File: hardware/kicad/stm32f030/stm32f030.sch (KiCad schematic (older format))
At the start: 5 parts, among them P1 CONN_01X02, U1 LM1117-3.3

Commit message: hardware/kicad/stm32f030: progress
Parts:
- P1: value CONN_01X02 -> 5VIN
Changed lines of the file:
@@
 P 4700 4500
 F 0 "P1" H 4700 4650 50  0000 C CNN
-F 1 "CONN_01X02" V 4800 4500 50  0000 C CNN
+F 1 "5VIN" V 4800 4500 50  0000 C CNN
 F 2 "Connectors:bornier2" H 4700 4500 50  0001 C CNN
 F 3 "" H 4700 4500 50  0000 C CNN

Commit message: hardware/kicad/stm32f030: adding eeprom step1
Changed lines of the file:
@@
 $Descr A4 11693 8268
 encoding utf-8
-Sheet 1 5
+Sheet 1 6
 Title ""
 Date ""
@@
 $EndComp
 $Comp
-L GND #PWR01
+L GND #PWR4
 U 1 1 5884B3C2
 P 5000 5000
-F 0 "#PWR01" H 5000 4750 50  0001 C CNN
+F 0 "#PWR4" H 5000 4750 50  0001 C CNN
 F 1 "GND" H 5000 4850 50  0000 C CNN
 F 2 "" H 5000 5000 50  0000 C CNN
@@
 $EndComp
 $Comp
-L +5V #PWR02
+L +5V #PWR1
 U 1 1 5884B3C8
 P 5000 4100
-F 0 "#PWR02" H 5000 3950 50  0001 C CNN
+F 0 "#PWR1" H 5000 3950 50  0001 C CNN
 F 1 "+5V" H 5000 4240 50  0000 C CNN
 F 2 "" H 5000 4100 50  0000 C CNN
@@
 $EndComp
 $Comp
-L GND #PWR03
+L GND #PWR6
 U 1 1 5884B8B0
 P 5750 5000
-F 0 "#PWR03" H 5750 4750 50  0001 C CNN
+F 0 "#PWR6" H 5750 4750 50  0001 C CNN
 F 1 "GND" H 5750 4850 50  0000 C CNN
 F 2 "" H 5750 5000 50  0000 C CNN
@@
 	5750 4800 5750 5000
 $Comp
-L +5V #PWR04
+L +5V #PWR2
 U 1 1 5884B8D9
 P 5400 4100
-F 0 "#PWR04" H 5400 3950 50  0001 C CNN
+F 0 "#PWR2" H 5400 3950 50  0001 C CNN
 F 1 "+5V" H 5400 4240 50  0000 C CNN
 F 2 "" H 5400 4100 50  0000 C CNN
@@
 	5400 4500 5450 4500
 $Comp
-L +3.3V #PWR05
+L +3.3V #PWR3
 U 1 1 5884B903
 P 6100 4100
-F 0 "#PWR05" H 6100 3950 50  0001 C CNN
+F 0 "#PWR3" H 6100 3950 50  0001 C CNN
 F 1 "+3.3V" H 6100 4240 50  0000 C CNN
 F 2 "" H 6100 4100 50  0000 C CNN
@@
 $EndComp
 $Comp
-L GND #PWR06
+L GND #PWR7
 U 1 1 5884BA4E
 P 6100 5000
-F 0 "#PWR06" H 6100 4750 50  0001 C CNN
+F 0 "#PWR7" H 6100 4750 50  0001 C CNN
 F 1 "GND" H 6100 4850 50  0000 C CNN
 F 2 "" H 6100 5000 50  0000 C CNN
@@
 $EndComp
 $Comp
-L GND #PWR07
+L GND #PWR5
 U 1 1 5884BA71
 P 5400 5000
-F 0 "#PWR07" H 5400 4750 50  0001 C CNN
+F 0 "#PWR5" H 5400 4750 50  0001 C CNN
 F 1 "GND" H 5400 4850 50  0000 C CNN
 F 2 "" H 5400 5000 50  0000 C CNN
@@
 Wire Wire Line
 	6400 3500 6700 3500
+$Sheet
+S 6750 4000 750  300
+U 589C1D7A
+F0 "EEPROM" 60
+F1 "eeprom.sch" 60
+F2 "scl" I L 6750 4100 60
+F3 "sda" B L 6750 4200 60
+$EndSheet
+Wire Wire Line
+	6750 4200 6500 4200
+Wire Wire Line
+	6500 4200 6500 3500
+Connection ~ 6500 3500
+Wire Wire Line
+	6750 4100 6600 4100
+Wire Wire Line
+	6600 4100 6600 3300
+Connection ~ 6600 3300
 $EndSCHEMATC

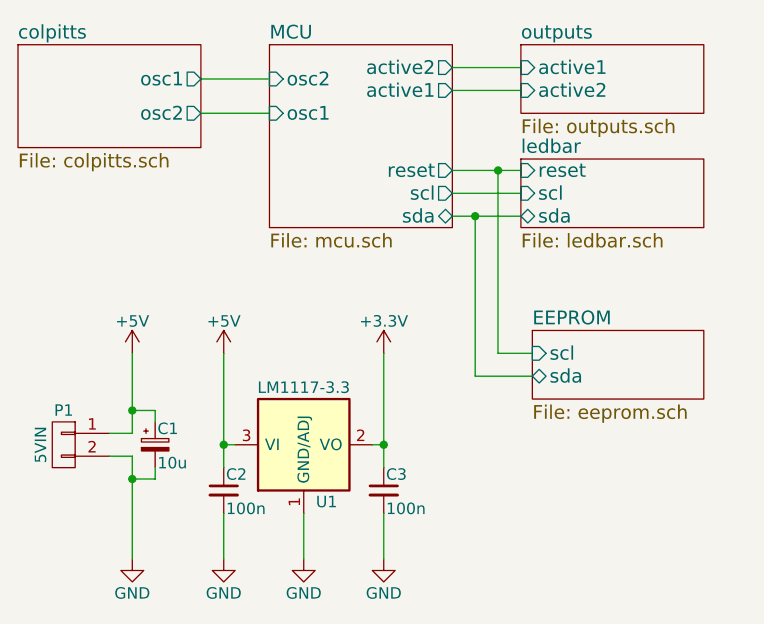
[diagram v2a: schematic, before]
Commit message: hardware/kicad/stm32f030: adding eeprom step2
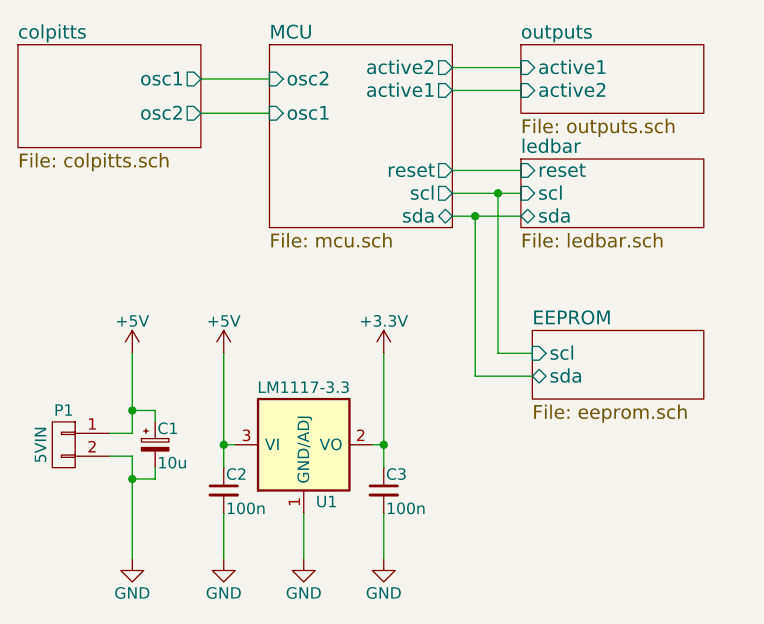
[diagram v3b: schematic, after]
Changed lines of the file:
@@
 	6750 4100 6600 4100
 Wire Wire Line
-	6600 4100 6600 3300
-Connection ~ 6600 3300
+	6600 4100 6600 3400
+Connection ~ 6600 3400
 $EndSCHEMATC

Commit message: hardware/kicad/stm32f030: final touches
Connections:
- net +5V: now also P1.2 (P2); no longer P1.1 (P1)
- net GND: now also P1.1 (P1); no longer P1.2 (P2)
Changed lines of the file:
@@
 F 3 "" H 4700 4500 50  0000 C CNN
 	1    4700 4500
-	-1   0    0    -1
+	-1   0    0    1
 $EndComp
 $Comp

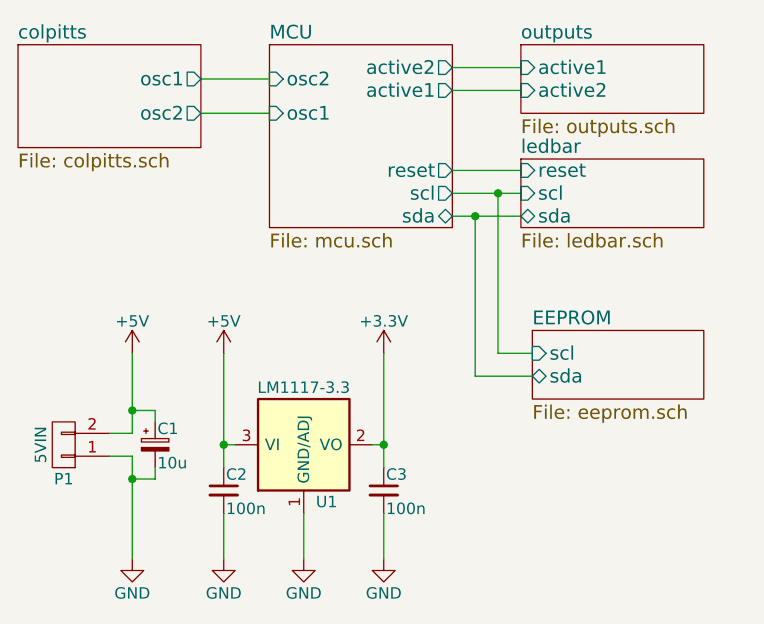
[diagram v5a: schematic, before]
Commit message: hardware/kicad/stm32f030: Ledbar removed, reorg started
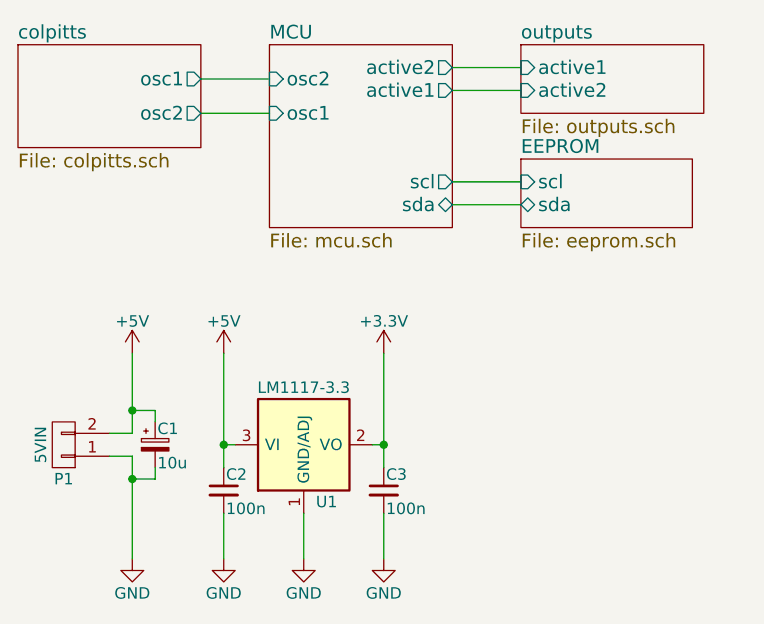
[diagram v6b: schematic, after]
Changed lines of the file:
@@
 Connection ~ 5000 4650
-$Sheet
-S 6700 3250 800  300
-U 58851FF0
-F0 "ledbar" 60
-F1 "ledbar.sch" 60
-F2 "scl" I L 6700 3400 60
-F3 "sda" B L 6700 3500 60
-F4 "reset" I L 6700 3300 60
-$EndSheet
 $Sheet
 S 5600 2750 800  800
@@
 F4 "osc1" I L 5600 3050 60
 F5 "osc2" I L 5600 2900 60
-F6 "scl" O R 6400 3400 60
-F7 "sda" B R 6400 3500 60
-F8 "reset" O R 6400 3300 60
+F6 "scl" O R 6400 3350 60
+F7 "sda" B R 6400 3450 60
 $EndSheet
-Wire Wire Line
-	6400 3300 6700 3300
-Wire Wire Line
-	6400 3400 6700 3400
-Wire Wire Line
-	6400 3500 6700 3500
 $Sheet
-S 6750 4000 750  300
+S 6700 3250 750  300
 U 589C1D7A
 F0 "EEPROM" 60
 F1 "eeprom.sch" 60
-F2 "scl" I L 6750 4100 60
-F3 "sda" B L 6750 4200 60
+F2 "scl" I L 6700 3350 60
+F3 "sda" B L 6700 3450 60
 $EndSheet
 Wire Wire Line
-	6750 4200 6500 4200
+	6400 3350 6700 3350
 Wire Wire Line
-	6500 4200 6500 3500
-Connection ~ 6500 3500
-Wire Wire Line
-	6750 4100 6600 4100
-Wire Wire Line
-	6600 4100 6600 3400
-Connection ~ 6600 3400
+	6400 3450 6700 3450
 $EndSCHEMATC

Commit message: hardware/kicad/stm32f030: blocks ready
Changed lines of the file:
@@
 $Descr A4 11693 8268
 encoding utf-8
-Sheet 1 6
+Sheet 1 5
 Title ""
 Date ""
@@
 F0 "outputs" 60
 F1 "outputs.sch" 60
-F2 "active1" I L 6700 2850 60
-F3 "active2" I L 6700 2950 60
-$EndSheet
-Wire Wire Line
-	5300 2900 5600 2900
-Wire Wire Line
-	5300 3050 5600 3050
+F2 "active1" I L 6700 2950 60
+F3 "active2" I L 6700 2850 60
+$EndSheet
 Wire Wire Line
 	6400 2850 6700 2850
@@
 F2 "active1" O R 6400 2950 60
 F3 "active2" O R 6400 2850 60
-F4 "osc1" I L 5600 3050 60
-F5 "osc2" I L 5600 2900 60
+F4 "osc1" I L 5600 2900 60
+F5 "osc2" I L 5600 3050 60
 F6 "scl" O R 6400 3350 60
 F7 "sda" B R 6400 3450 60
@@
 Wire Wire Line
 	6400 3450 6700 3450
+Wire Wire Line
+	5300 3050 5600 3050
+Wire Wire Line
+	5300 2900 5600 2900
 $EndSCHEMATC
